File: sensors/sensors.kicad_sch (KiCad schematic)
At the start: 3 parts, among them J1 GPIO, J2 JP1115CH1&2, J3 Conn_01x16

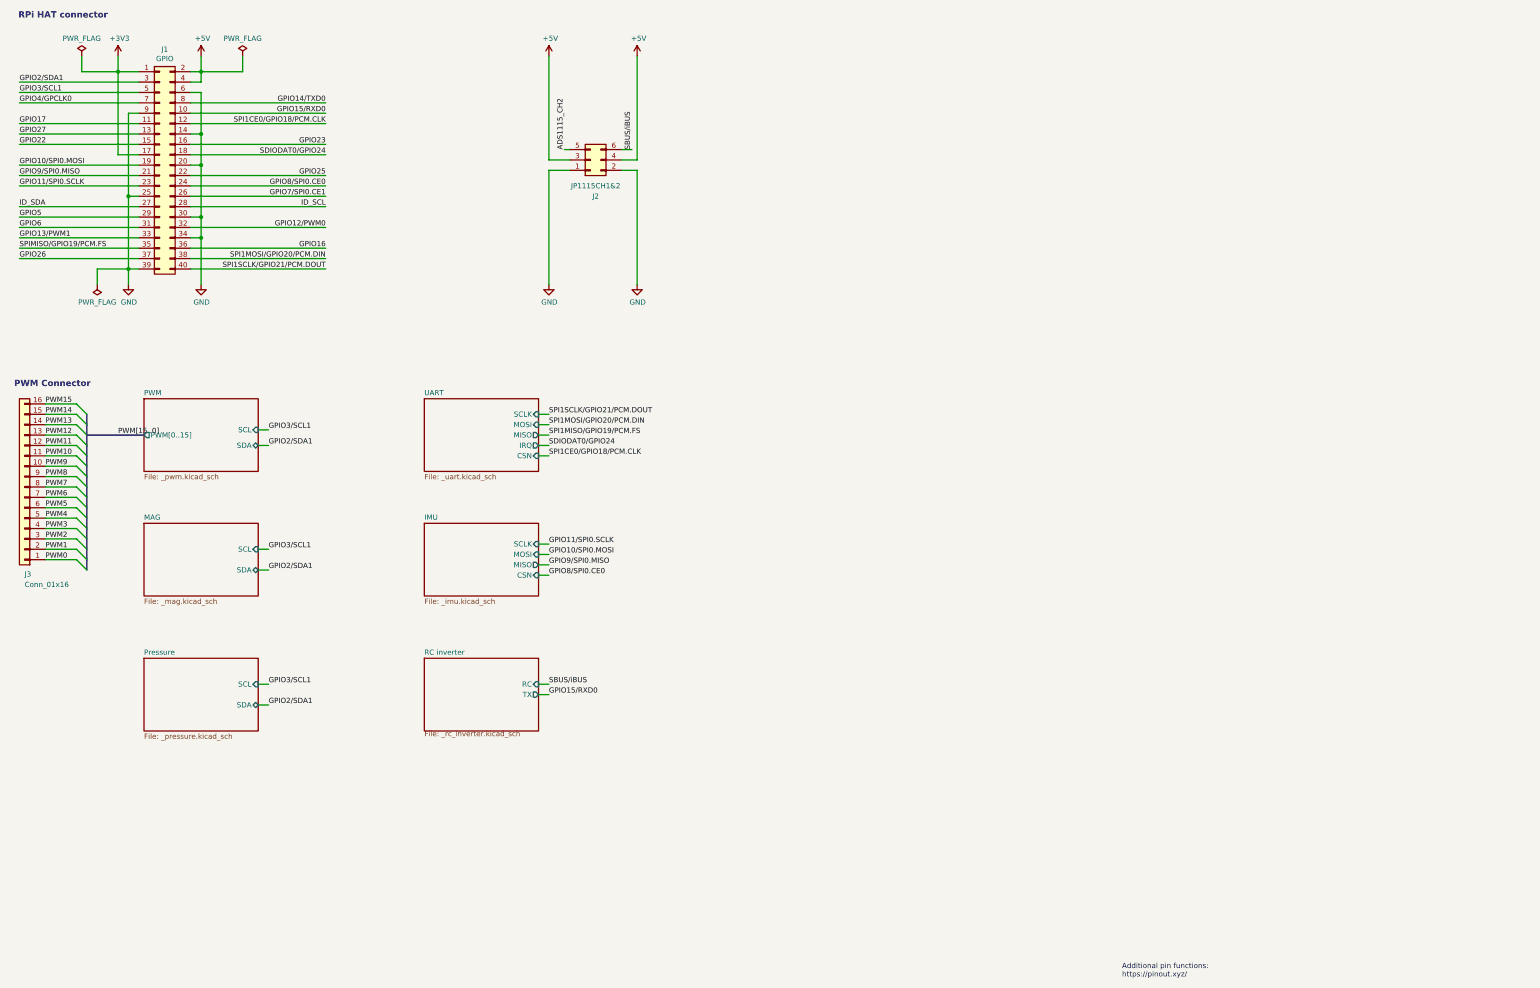
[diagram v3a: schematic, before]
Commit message: add ADC
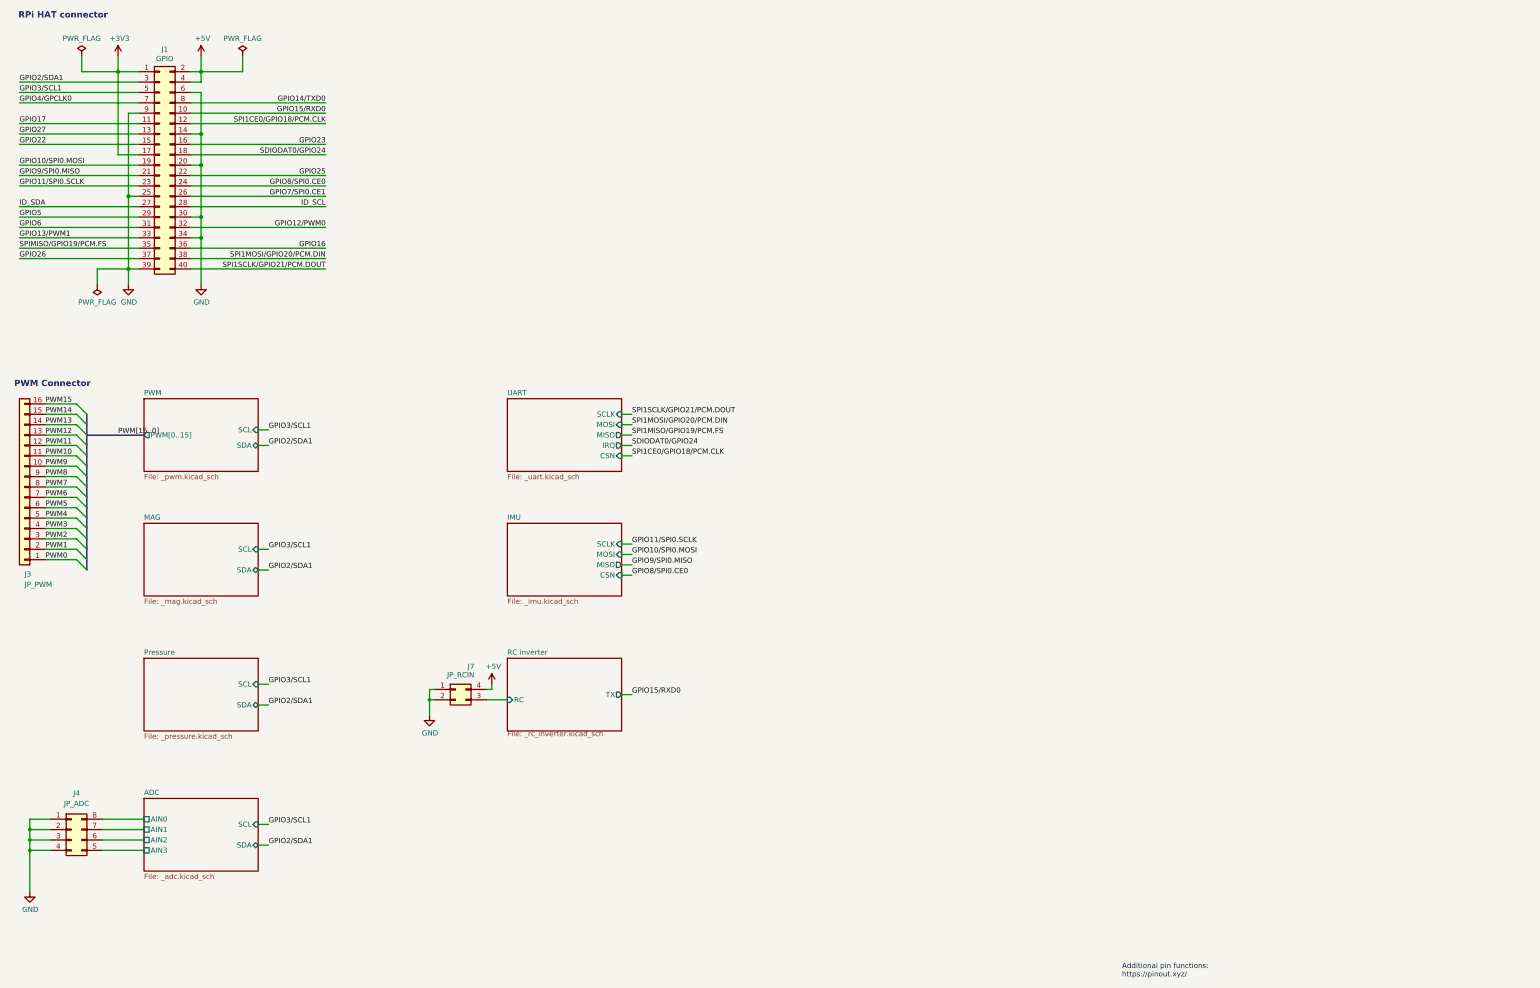
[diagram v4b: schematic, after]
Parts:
- removed J2: JP1115CH1&2, Connector_PinHeader_2.54mm:PinHeader_2x03_P2.54mm_Horizontal, symbol Connector_Generic:Conn_02x03_Odd_Even
- added J4: JP_ADC, Connector_PinHeader_2.54mm:PinHeader_2x04_P2.54mm_Horizontal, symbol Connector_Generic:Conn_02x04_Counter_Clockwise
- added J7: JP_RCIN, Connector_PinHeader_2.54mm:PinHeader_2x02_P2.54mm_Horizontal, symbol Connector_Generic:Conn_02x02_Counter_Clockwise
- J3: value Conn_01x16 -> JP_PWM
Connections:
- net +5V: now also J7.4 (Pin_4)
- net GND: now also J4.1 (Pin_1), J4.2 (Pin_2), J4.3 (Pin_3), J4.4 (Pin_4), J7.1 (Pin_1), J7.2 (Pin_2)
- new net ADC/AIN0: J4.8 (Pin_8)
- new net ADC/AIN1: J4.7 (Pin_7)
- new net ADC/AIN2: J4.6 (Pin_6)
- new net ADC/AIN3: J4.5 (Pin_5)
- new net RC inverter/RC: J7.3 (Pin_3)
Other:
- added sheet ADC (_adc.kicad_sch)

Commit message: add boot mode switch
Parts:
- added R33, R34: 3.3KΩ (3301) ±1%, Resistor_SMD:R_0402_1005Metric, symbol Device:R
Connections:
- net SPIMISO/GPIO19/PCM.FS is gone; now on net SPI1MISO/GPIO19/PCM.FS: J1.35 (Pin_35)
- net +3V3: now also R33.1, R34.1
- net GPIO2/SDA1: now also R33.2
- net GPIO3/SCL1: now also R34.2
- no-connect marks 0 -> 15
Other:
- added sheet Boot mode (_boot_mode.kicad_sch)
- note added: "I2C pullup"
- moved on the sheet: J7

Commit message: routing
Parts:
- removed J4: JP_ADC, Connector_PinHeader_2.54mm:PinHeader_2x04_P2.54mm_Horizontal, symbol Connector_Generic:Conn_02x04_Counter_Clockwise
- removed J7: JP_RCIN, Connector_PinHeader_2.54mm:PinHeader_2x02_P2.54mm_Horizontal, symbol Connector_Generic:Conn_02x02_Counter_Clockwise
- added J4: JP_ADC, Connector_PinHeader_2.54mm:PinHeader_2x06_P2.54mm_Horizontal, symbol Connector_Generic:Conn_02x06_Odd_Even
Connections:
- net +5V: now also J4.11 (Pin_11)
- net ADC/AIN0: now also J4.1 (Pin_1)
- net ADC/AIN1: now also J4.3 (Pin_3)
- net ADC/AIN2: now also J4.5 (Pin_5)
- net ADC/AIN3: now also J4.7 (Pin_7)
- net GND: now also J4.10 (Pin_10), J4.12 (Pin_12), J4.2 (Pin_2), J4.4 (Pin_4), J4.6 (Pin_6), J4.8 (Pin_8)
- new net RCIN: J4.9 (Pin_9)

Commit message: intermediate commit
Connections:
- no-connect marks 15 -> 14
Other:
- added sheet Buzzer (_buzzer.kicad_sch)
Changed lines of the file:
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@@
 (kicad_sch
-	(version 20260623)
+	(version 20251012)
 	(generator "eeschema")
-	(generator_version "10.99")
+	(generator_version "10.00")
 	(paper "A3")
 	(title_block
@@
 	)
 	(no_connect
-		(at 73.66 74.93)
-	)
-	(no_connect
 		(at 73.66 67.31)
 	)
@@
 	(wire
 		(pts
+			(xy 294.64 189.23) (xy 297.18 189.23)
+		)
+		(stroke
+			(width 0)
+			(type default)
+		)
+	)
+	(wire
+		(pts
 			(xy 54.61 214.63) (xy 54.61 212.09)
 		)
@@
 		)
 	)
+	(label "GPIO12{slash}PWM0"
+		(at 297.18 189.23 0)
+		(effects
+			(font
+				(size 1.27 1.27)
+			)
+			(justify left bottom)
+		)
+	)
 	(label "GPIO17"
 		(at 31.75 49.53 0)
@@
 				)
 			)
+		)
+	)
+	(sheet
+		(at 266.7 180.34)
+		(size 27.94 17.78)
+		(exclude_from_sim no)
+		(in_bom yes)
+		(on_board yes)
+		(dnp no)
+		(fields_autoplaced yes)
+		(stroke
+			(width 0.1524)
+			(type solid)
+		)
+		(fill
+			(color 0 0 0 0)
+		)
+		(property "Sheetname" "Buzzer"
+			(at 266.7 179.6284 0)
+			(show_name no)
+			(do_not_autoplace no)
+			(effects
+				(font
+					(size 1.27 1.27)
+				)
+				(justify left bottom)
+			)
+		)
+		(property "Sheetfile" "_buzzer.kicad_sch"
+			(at 266.7 198.7046 0)
+			(show_name no)
+			(do_not_autoplace no)
+			(effects
+				(font
+					(size 1.27 1.27)
+				)
+				(justify left top)
+			)
+		)
+		(pin "PWM" input
+			(at 294.64 189.23 0)
+			(effects
+				(font
+					(size 1.27 1.27)
+				)
+				(justify right)
+			)
+		)
+		(instances
+			(project "sensors"
+				(path "/e63e39d7-6ac0-4ffd-8aa3-1841a4541b55"
+					(page "10")
+				)
+			)
